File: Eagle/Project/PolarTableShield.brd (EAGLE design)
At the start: 55.9 x 59.7 mm, 45 parts, among them IC2 LM358D, J1 Pi Power Jack, J10 LED + Radio, J2 Header - Right angled, female, J3 Pi Connection, J4 extra points, J5 IR Sensors, J6 Switch A + B, J7 Switch C + D, J8 Switch E + F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

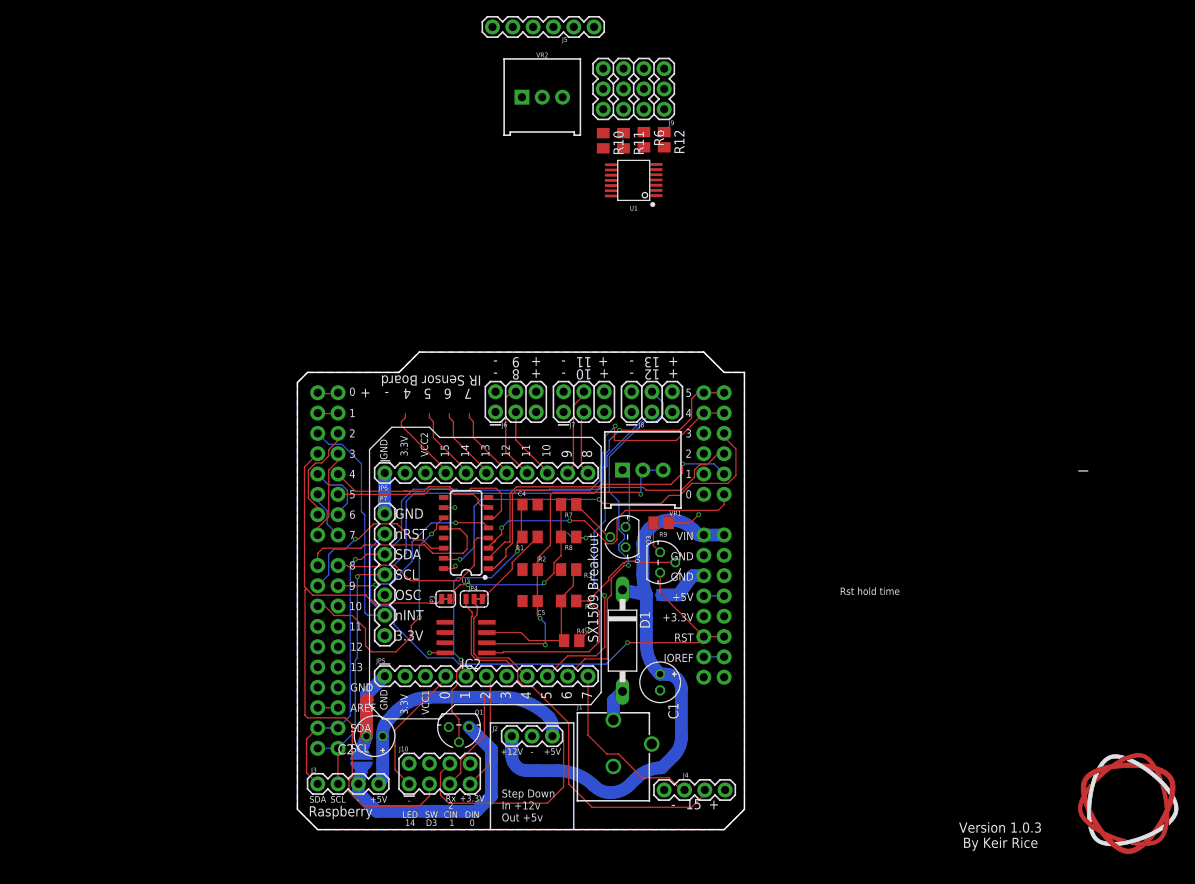
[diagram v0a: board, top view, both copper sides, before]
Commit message: Expanded board
Remove my self imposed footprint restriction.
Add circuit for analog to 1bit digital signal for the IR sensors.
Added the new SX1509 custom device.
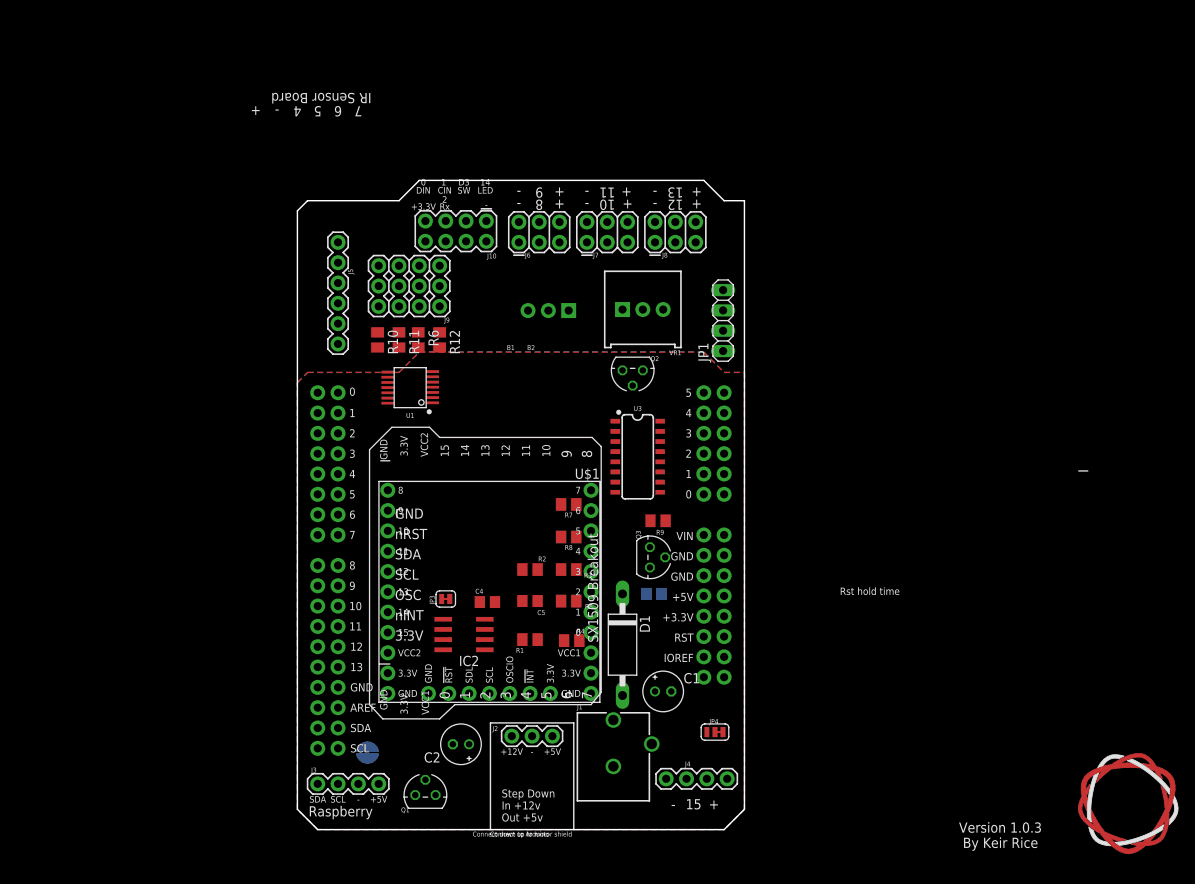
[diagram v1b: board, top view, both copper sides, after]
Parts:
- removed JP5: Left Sub-board Mount, keir_library:1X11
- removed JP6: Right Sub-board Mount, keir_library:1X11
- removed JP7: Top Sub-board Mount, keir_library:1X07
- added JP1: (no value), pinhead:1X04
- added U$1: SX1509, keir_library:SX1509
- moved J10 67.8 mm to (19.8, 74.8), turned to 180 degrees
- moved J5 44.1 mm to (5.08, 60.7), turned to 90 degrees
- moved U1 38.1 mm to (14.1, 55.2)
- moved R6 37.7 mm to (15.1, 61.2)
- moved R10 37.6 mm to (10.0, 61.2)
- moved R12 37.6 mm to (17.8, 61.2)
- moved R11 37.5 mm to (12.7, 61.2)
- moved J9 37.3 mm to (17.8, 65.4)
- moved JP4 34.4 mm to (52.2, 12.2)
- moved VR2 26.7 mm to (31.4, 64.9), flipped to the bottom
- moved U3 23.5 mm to (42.5, 46.6), turned to 270 degrees
- moved J6 21.4 mm to (27.7, 73.4)
- moved J7 21.4 mm to (36.2, 73.4)
- moved J8 21.4 mm to (44.7, 73.4)
- moved Q2 20.8 mm to (41.9, 57.4), turned to 180 degrees
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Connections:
- removed net B0: J10.1, JP5.4
- removed net B10: J6.3, JP6.9
- removed net B11: J6.4, JP6.8
- removed net B12: J9.2, JP6.7, R12.1, U1.1
- removed net B13: J9.5, JP6.6, R6.1, U1.2
- removed net B14: J9.8, JP6.5, R11.1, U1.14
- removed net B15: J9.11, JP6.4, R10.1, U1.13
- removed net B5: J8.3, JP5.9
- removed net B6: J8.4, JP5.10
- removed net B8: J7.3, JP6.11
- removed net B9: J7.4, JP6.10
- removed net NINT: B1.D2, JP7.6
- removed net RES: B1.RES, B2.RES, JP7.2, Q3.1
- new net !INT: B1.D2, U$1.I6
- new net !RES: B1.RES, B2.RES, Q3.1, U$1.I2
- new net B1: U$1.O1
- new net B2: U$1.O2
- new net B3: U$1.O3
- new net IR_G: J9.2, R12.1, U$1.O15, U1.1
- new net IR_H: J9.5, R6.1, U$1.O14, U1.2
- new net IR_I: J9.8, R11.1, U$1.O13, U1.14
- new net IR_J: J9.11, R10.1, U$1.O12, U1.13
- new net N$18: B1.A2, JP1.3
- new net N$19: B1.A1, JP1.2
- new net N$20: B1.A0, JP1.1
- new net N$6: B1.A3, JP1.4
- new net SW_A: J6.3, U$1.O11
- new net SW_B: J6.4, U$1.O10
- new net SW_C: J7.3, U$1.O9
- new net SW_D: J7.4, U$1.O8
- new net SW_E: J8.3, U$1.O6
- new net SW_F: J8.4, U$1.O7
- new net VCC1: U$1.P3
- new net VCC2: U$1.P4
- new net WAKE_LED: J10.1, U$1.O5
- net 3.3V: now also U$1.I1, U$1.P2, U$1.P5; no longer JP5.2, JP6.2, JP7.7
- net B4: now also U$1.O4; no longer JP5.8
- net B7: now also U$1.O0; no longer J4.3, JP5.11
- net GND: now also U$1.I7, U$1.P1, U$1.P6; no longer JP5.1, JP6.1, JP7.1
- net SCL: now also U$1.I4; no longer JP7.4
- net SDA: now also U$1.I3; no longer JP7.3
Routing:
- net SDA: track 94.7 -> 0.00 mm, vias 2 -> 0
- net SCL: track 92.8 -> 0.00 mm, vias 2 -> 0
- net D3_WAKE_SW: track 81.3 -> 0.00 mm
- net 12V: track 71.7 -> 0.00 mm
- net RES: track 69.4 -> 0.00 mm, vias 1 -> 0
- net 15_PLUG: track 51.0 -> 0.00 mm
- net SLEEPX: track 50.2 -> 0.00 mm, vias 2 -> 0
- net B6: track 46.5 -> 0.00 mm, vias 1 -> 0
- net N$8: track 46.2 -> 0.00 mm, vias 3 -> 0
- net B5: track 41.7 -> 0.00 mm, vias 1 -> 0
- net ENX: track 41.2 -> 0.00 mm
- net SLEEPY: track 39.1 -> 0.00 mm, vias 1 -> 0
- net ENY: track 37.6 -> 0.00 mm, vias 2 -> 0
- net N$2: track 37.2 -> 0.00 mm, vias 2 -> 0
- net COMP_OUT: track 35.2 -> 0.00 mm
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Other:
- board size 55.9 x 59.7 mm -> 55.9 x 81.2 mm

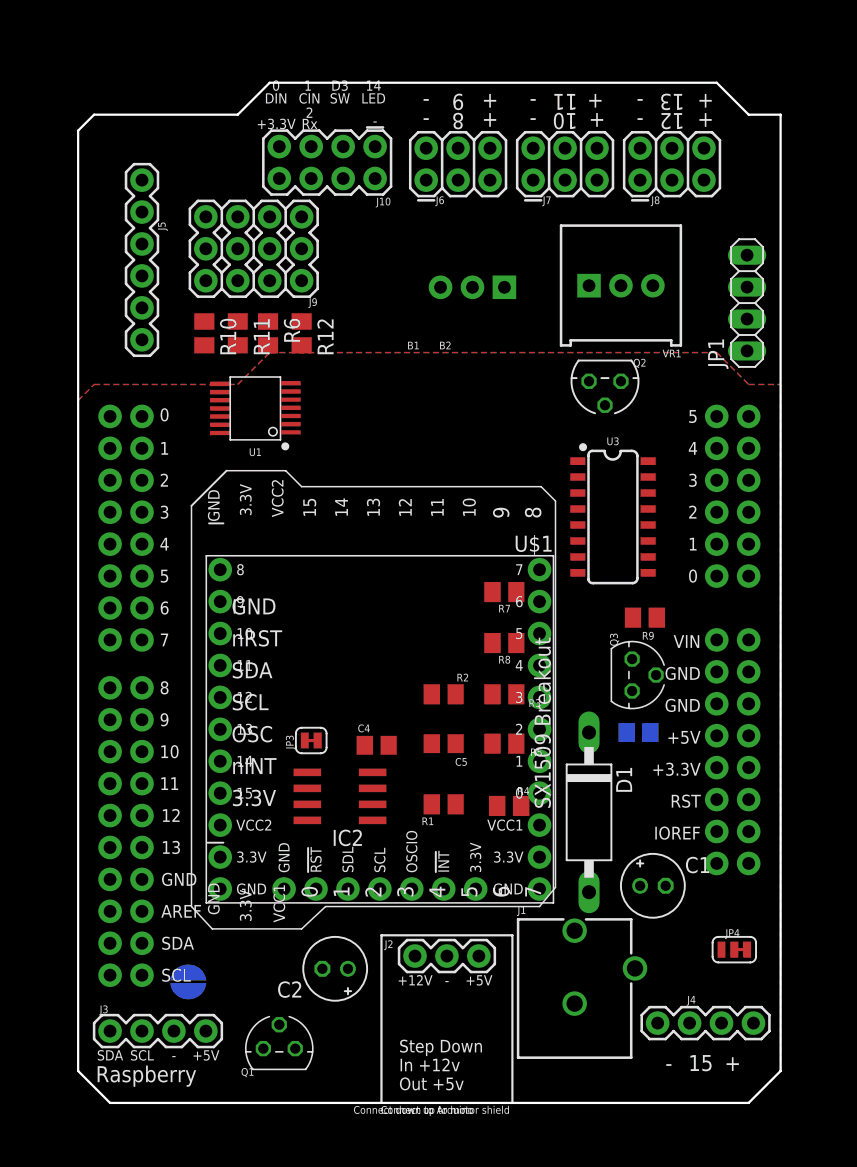
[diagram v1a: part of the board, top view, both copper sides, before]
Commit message: Back to normal shield size
Removed the sensor analog to digital section.
Added more specific net classes to be explicit about the logic voltage levels of the different boards.
Added 3.3V to 5V logic conversion for the I2C bus.
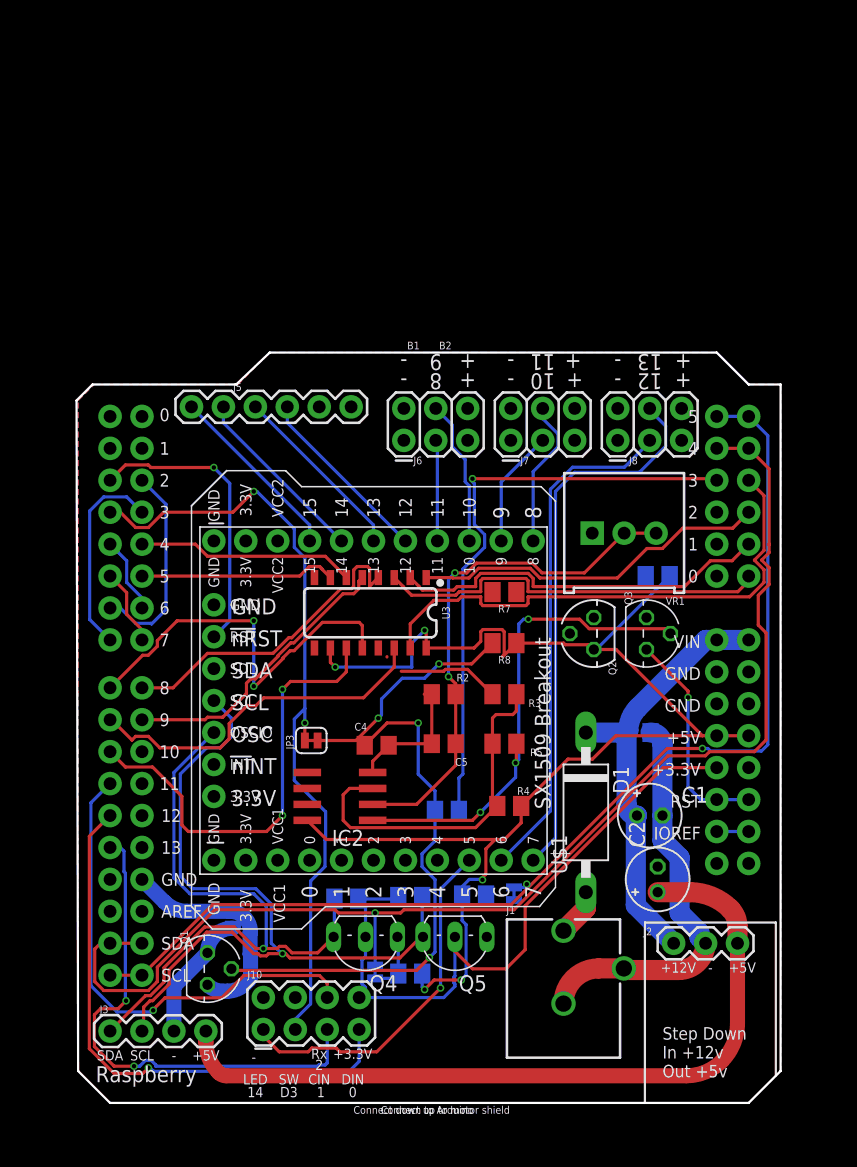
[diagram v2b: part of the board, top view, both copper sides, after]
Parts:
- removed J4: extra points, keir_library:1X04_1.24MM_RA_MALE
- removed J9: (no value), keir_library:3X04_1.24MM_RA_MALE
- removed JP1: (no value), pinhead:1X04
- removed JP4: Route 15 to external, SparkFun-Jumpers:SMT-JUMPER_3_1-NC_TRACE_SILK
- removed U1: LM339PWR, SparkFun-IC-Amplifiers:TSSOP-14
- removed VR2: 10k, SparkFun-Resistors:TRIMPOT-PTH-3386U
- added JP5, JP6: (no value), SparkFun-Jumpers:SMT-JUMPER_2_NC_TRACE_NO-SILK
- added Q4, Q5: 2N7000, keir_library:TO92-
- JP2: device SparkFun-Jumpers:SMT-JUMPER_2_NO_SILK_ROUND -> SparkFun-Jumpers:SMT-JUMPER_2_NO_SILK
- R10, R11, R12, R6: value 221k -> 4.7k
- moved J10 67.7 mm to (18.5, 7.11), turned to 0 degrees
- moved R6 52.2 mm to (26.4, 10.3), flipped to the bottom, turned to 0 degrees
- moved R10 49.6 mm to (31.5, 16.5), flipped to the bottom, turned to 180 degrees
- moved R11 46.9 mm to (26.4, 16.4), flipped to the bottom, turned to 180 degrees
- moved R12 45.1 mm to (21.3, 16.3), flipped to the bottom, turned to 0 degrees
- moved C2 26.6 mm to (46.1, 17.8), turned to 90 degrees
- moved J6 20.8 mm to (25.9, 52.7)
- moved J7 20.8 mm to (34.4, 52.7)
- moved J8 20.8 mm to (42.9, 52.7)
- moved U3 20.8 mm to (23.2, 39.0), turned to 180 degrees
- moved J2 20.6 mm to (47.4, 12.7)
- moved Q2 20.1 mm to (41.0, 37.3), turned to 90 degrees
- moved VR1 19.7 mm to (43.4, 45.3)
- moved J5 17.5 mm to (21.7, 55.4), turned to 180 degrees
- moved Q1 8.54 mm to (10.3, 10.7), turned to 270 degrees
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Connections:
- net 12V renamed 12V_SUPPLY
- net PI_5V renamed 5V_SUPPLY
- removed net 15_PLUG: J4.2, JP4.1
- removed net N$10: J9.6, U1.4
- removed net N$11: J5.4, J9.7
- removed net N$12: J9.12, U1.10
- removed net N$13: J9.9, U1.8
- removed net N$14: J9.3, U1.6
- removed net N$15: J5.5, J9.4
- removed net N$16: J5.3, J9.10
- removed net N$17: R10.2, R11.2, R12.2, R6.2, U1.11, U1.5, U1.7, U1.9, VR2.2
- removed net N$18: B1.A2, JP1.3
- removed net N$19: B1.A1, JP1.2
- removed net N$20: B1.A0, JP1.1
- removed net N$9: J5.6, J9.1
- removed net VCC1: U$1.P3
- removed net VCC2: U$1.P4
- new net A0: B1.A0
- new net A1: B1.A1
- new net A2: B1.A2
- new net SCL_3V: J3.3, Q5.1, R11.2, U$1.I4
- new net SCL_5V: JP6.1, Q5.3, R10.2
- new net SDA_3V: J3.4, Q4.1, R12.2, U$1.I3
- new net SDA_5V: JP5.1, Q4.3, R6.2
- net !RES: no longer U$1.I2
- net 3.3V: now also Q4.2, Q5.2, R11.1, R12.1; no longer IC2.8, J4.1, Q2.E, R4.2, R8.1, R9.1, U$1.P2, U$1.P5, U1.3, U3.10, U3.16, VR2.1
- net 5V: now also IC2.8, Q2.E, R10.1, R4.2, R6.1, R8.1, R9.1, U3.10, U3.16
- net B4: no longer JP4.2
- net GND: no longer C1.-, C9.2, J1.GND, J1.GNDBREAK, J2.2, J4.4, U$1.P1, U$1.P6, U1.12, VR2.3
- net IR_G: now also J5.6; no longer J9.2, R12.1, U1.1
- net IR_H: now also J5.5; no longer J9.5, R6.1, U1.2
- net IR_I: now also J5.4; no longer J9.8, R11.1, U1.14
- net IR_J: now also J5.3; no longer J9.11, R10.1, U1.13
- net N$6: now also C1.-, C9.2, J1.GND, J1.GNDBREAK, J2.2; no longer B1.A3, JP1.4
- net PIPOWER_SIGNAL: now also B1.A3; no longer JP4.3
- net SCL: now also JP6.2; no longer J3.3, U$1.I4
- net SDA: now also JP5.2; no longer J3.4, U$1.I3
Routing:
- net 5V: track 0.00 -> 107.6 mm, vias 0 -> 5
- net SDA: track 0.00 -> 101.1 mm, vias 0 -> 1
- net SCL: track 0.00 -> 90.5 mm, vias 0 -> 2
- net D3_WAKE_SW: track 0.00 -> 62.7 mm, vias 0 -> 2
- net 5V_SUPPLY: track 0.00 -> 62.3 mm
- net SCL_3V: track 0.00 -> 61.6 mm, vias 0 -> 1
- net 3.3V: track 0.00 -> 55.0 mm
- net SDA_3V: track 0.00 -> 51.1 mm, vias 0 -> 1
- net PIPOWER_SIGNAL: track 0.00 -> 47.3 mm, vias 0 -> 1
- net D12_SDIN: track 0.00 -> 44.7 mm, vias 0 -> 1
- net SW_F: track 0.00 -> 43.9 mm
- net SLEEPX: track 0.00 -> 41.9 mm
- net N$8: track 0.00 -> 41.6 mm, vias 0 -> 2
- net N$2: track 0.00 -> 41.5 mm, vias 0 -> 2
- net D13_SCIN: track 0.00 -> 41.1 mm, vias 0 -> 2
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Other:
- board size 55.9 x 81.2 mm -> 56 x 59.7 mm
